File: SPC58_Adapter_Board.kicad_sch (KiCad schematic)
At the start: 6 parts, among them U1 SPC58NN84E7RMHBR

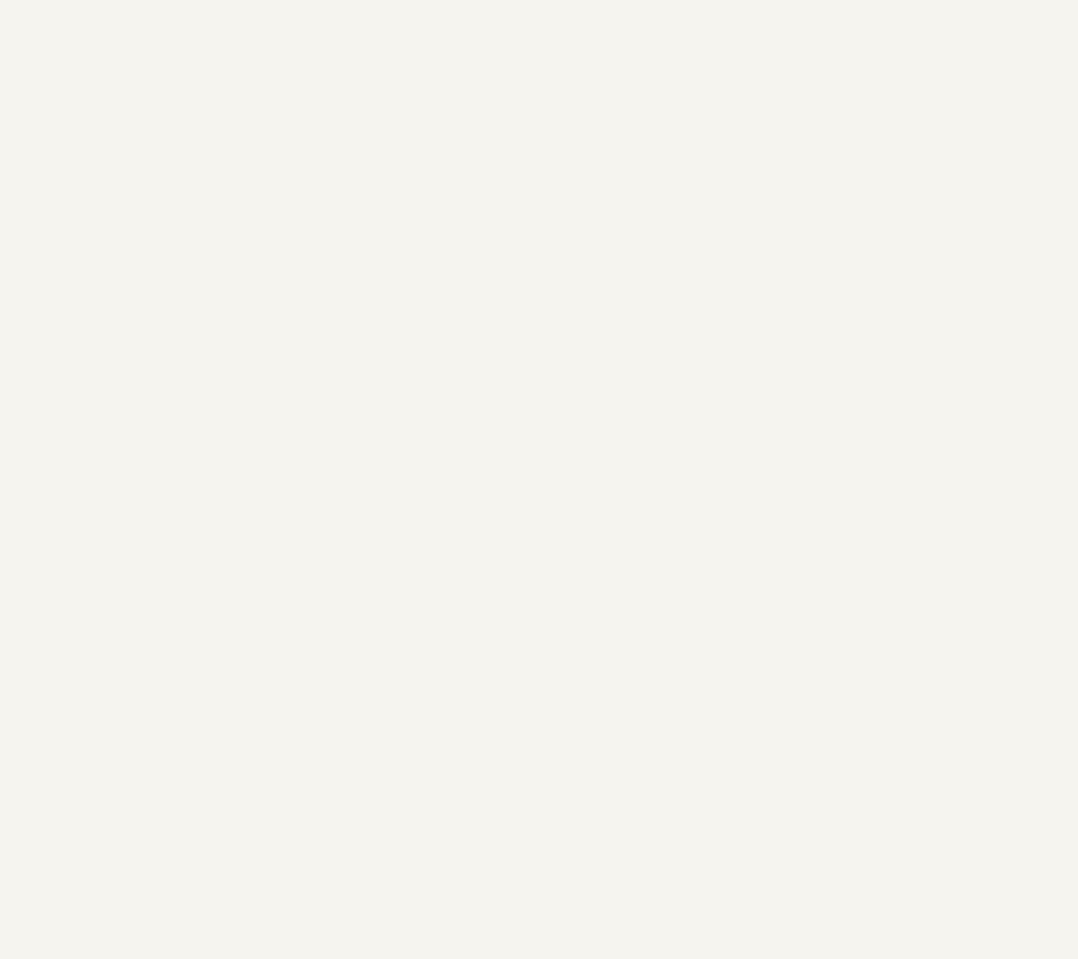
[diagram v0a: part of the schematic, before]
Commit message: Added symbol and footprint for CW308 connector
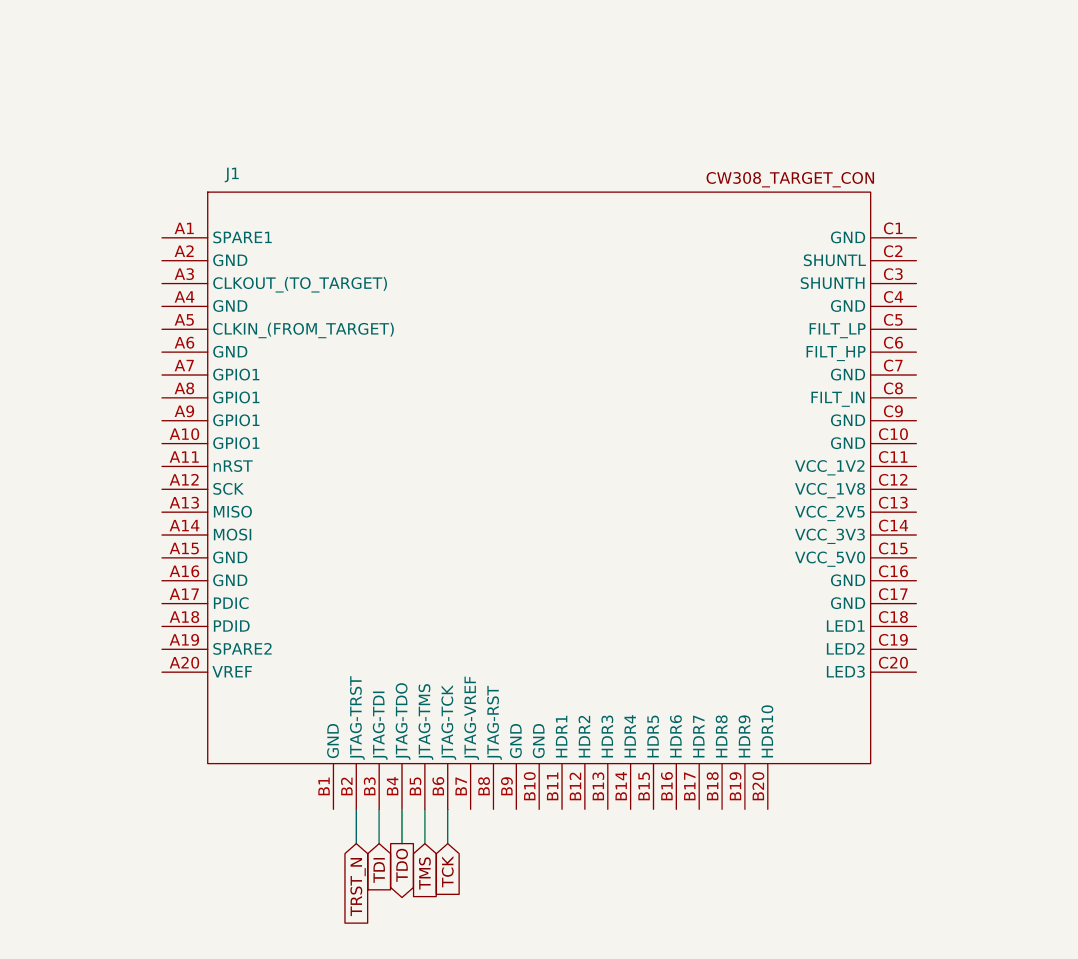
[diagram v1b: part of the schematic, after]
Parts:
- added J1: ~, My_Library:CW308_TARGET_CON, symbol My_Library:CW308_TARGET_CON
- U1: footprint LQFP_RMHBR_STM -> footprints:LQFP_RMHBR_STM-L
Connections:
- net TCK: now also J1.B6 (JTAG-TCK)
- net TDI: now also J1.B3 (JTAG-TDI)
- net TDO: now also J1.B4 (JTAG-TDO)
- net TMS: now also J1.B5 (JTAG-TMS)
- net TRST_N: now also J1.B2 (JTAG-TRST)

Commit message: Development of power source
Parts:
- removed R1, R2, R3, R4: 0, symbol Device:R
- added C22: 2.2uF, symbol Device:C
- added C23: 100nF, symbol Device:C
- added JP1: Jumper_2_Bridged, symbol Jumper:Jumper_2_Bridged
- added JP2, JP3: Jumper_2_Open, symbol Jumper:Jumper_2_Open
- added R6, R7: 10K, symbol Device:R
- added R8: 1R0, symbol Device:R
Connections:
- net VDD_LV is gone; now on net VCC_INT_SHUNTLOW: U1.100 (VDD_LV), U1.123 (VDD_LV), U1.24 (VDD_LV), U1.68 (VDD_LV)
- net GND: now also J1.A15 (GND), J1.A16 (GND), J1.A2 (GND), J1.A4 (GND), J1.A6 (GND), J1.B1 (GND), J1.B10 (GND), J1.B9 (GND), J1.C1 (GND), J1.C10 (GND), J1.C16 (GND), J1.C17 (GND), J1.C4 (GND), J1.C7 (GND), J1.C9 (GND), U1.118 (TESTMODE), C22.2, C23.2
- net JCOMP: now also J1.B11 (HDR1)
- net VDD_HV: now also R6.1, R7.1
- net VDD_IO_MAIN: now also J1.B7 (JTAG-VREF)
- net RESET: now reaches U1.121 (PORST)
- net RESET: now also J1.A11 (nRST), J1.B8 (JTAG-RST), U1.122 (ESR0), R6.2, R7.2
- net VCC_INT_SHUNTLOW: now reaches J1.C2 (SHUNTL)
- net VCC_INT_SHUNTLOW: now also R8.1
- net VCC_INT_CORE: now reaches J1.C3 (SHUNTH)
- net VCC_INT_CORE: now also JP1.2 (B), JP3.2 (B)
- net at J1.C5 (FILT_LP): now also J1.C6 (FILT_HP), JP2.1 (A)
- net at J1.C8 (FILT_IN): now also JP3.1 (A)
- new net: C22.1, C23.1, JP1.1 (A), JP2.2 (B), R8.2

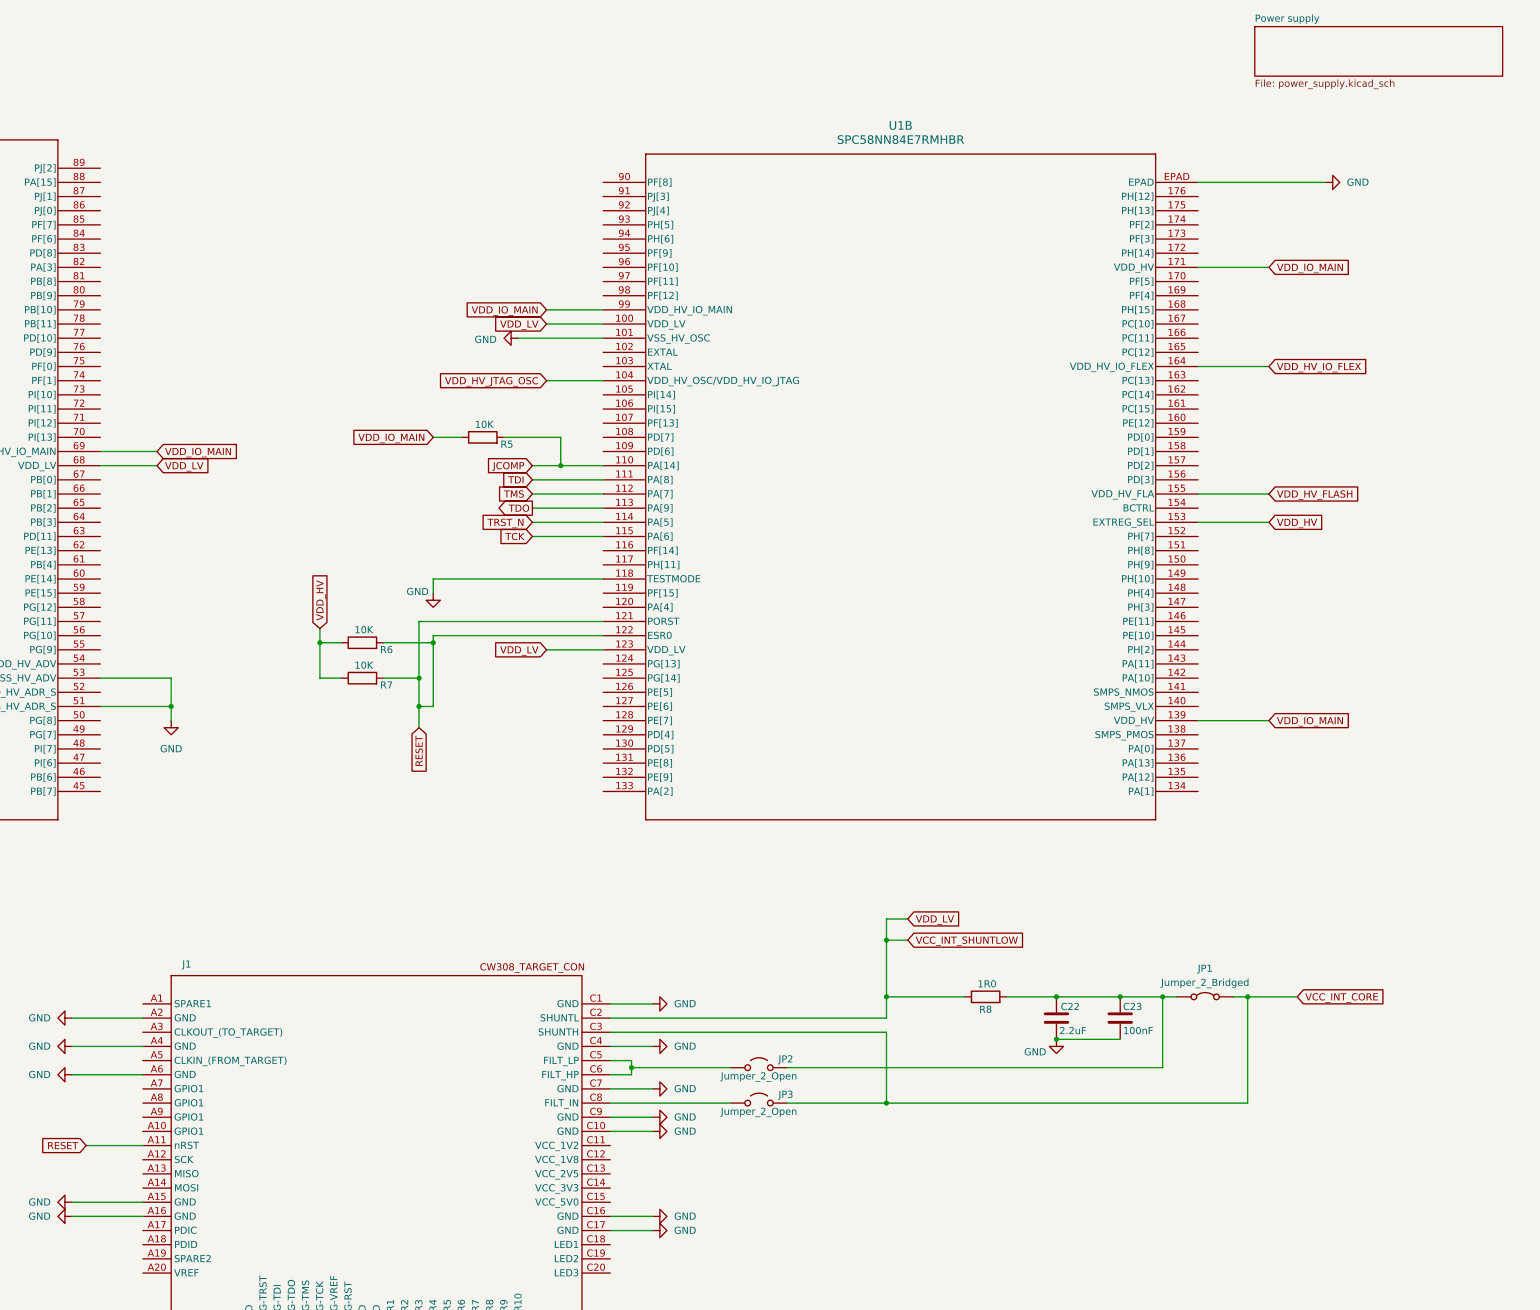
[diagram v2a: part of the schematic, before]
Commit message: Added CAN Bus schematic
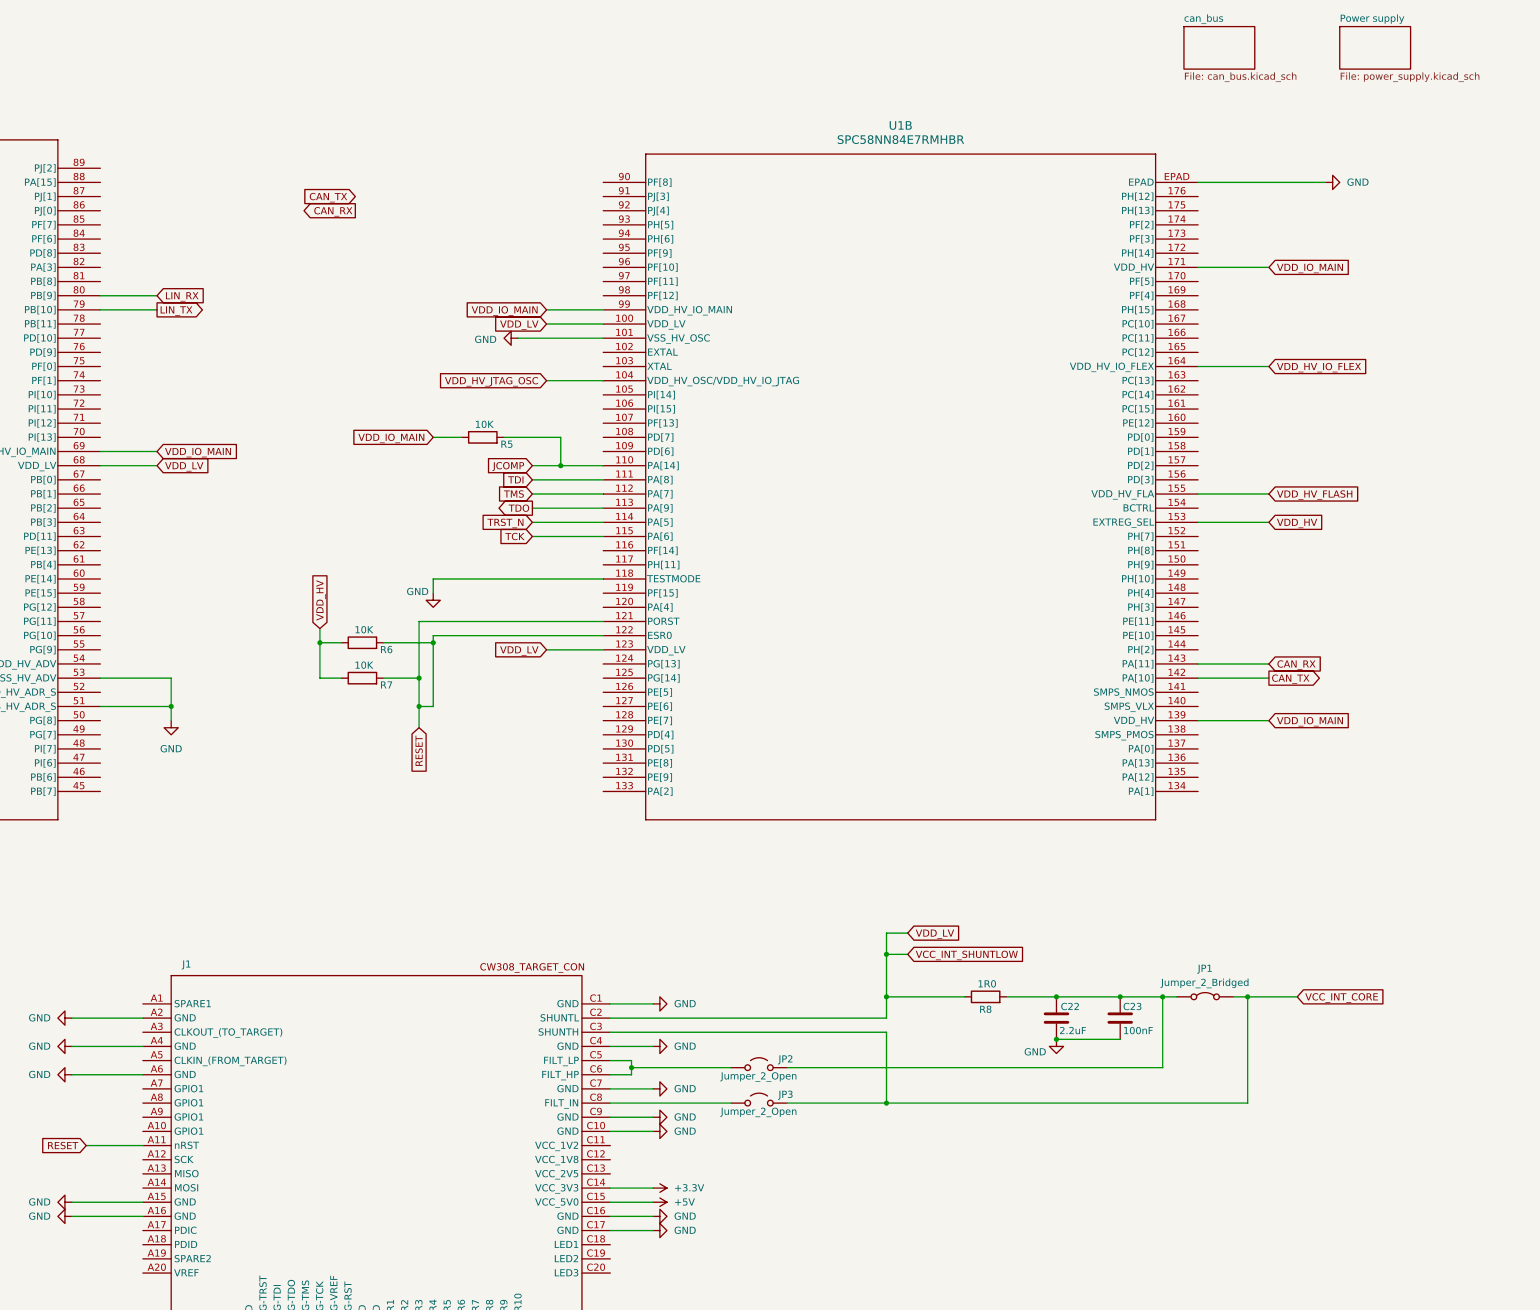
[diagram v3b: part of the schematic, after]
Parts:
- J1: value ~ -> (none)
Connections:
- net CAN_TX: now reaches U1.142 (PA[10])
- net CAN_RX: now reaches U1.143 (PA[11])
- net +3.3V: now reaches J1.C14 (VCC_3V3)
- net +5V: now reaches J1.C15 (VCC_5V0)
- net LIN_TX: now reaches U1.79 (PB[10])
- net LIN_RX: now reaches U1.80 (PB[9])
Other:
- added sheet can_bus (can_bus.kicad_sch)

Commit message: Development backup
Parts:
- added C32, C33, C34, C35: DNF, symbol Device:C
- added JP10, JP7, JP8, JP9: VDD_LV_JUMPER, symbol Jumper:Jumper_2_Small_Open
- added R12, R13, R14: 0R, symbol Device:R
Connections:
- net GND: now also R14.2; no longer U1.118 (TESTMODE)
- net RESET: now also R12.1, R13.2; no longer R6.2, R7.2, U1.121 (PORST), U1.122 (ESR0)
- net VCC_INT_SHUNTLOW: now also C32.1, C33.1, C34.1, C35.1, JP10.1 (A), JP7.1 (A), JP8.2 (B), JP9.1 (A); no longer U1.100 (VDD_LV), U1.123 (VDD_LV), U1.24 (VDD_LV), U1.68 (VDD_LV)
- new net: JP9.2 (B), U1.100 (VDD_LV)
- new net: R14.1, U1.118 (TESTMODE)
- new net: R13.1, R7.2, U1.121 (PORST)
- new net: R12.2, R6.2, U1.122 (ESR0)
- new net: JP10.2 (B), U1.123 (VDD_LV)
- new net: C32.2, C33.2, C34.2, C35.2
- new net: JP7.2 (B), U1.24 (VDD_LV)
- new net: JP8.1 (A), U1.68 (VDD_LV)
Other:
- note added: "Disable use of SMPS"
- note added: "VDD_LV_JUMPER must be soldered based on the test you want to execute, at least one must be soldered otherwise CORE is not powered"
- moved on the sheet: R6, R7
